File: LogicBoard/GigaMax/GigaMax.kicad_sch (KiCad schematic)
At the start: 40 parts, among them SW1 BOOT, SW3 RST, U12 STM32F407VGT6, U14 LM4128AMF-3.3, Y1 X50328MSB2GI

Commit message: moved libs and gigamax version
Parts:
- R2: footprint Resistor_SMD:R_0805_2012Metric -> Resistor_SMD:R_0603_1608Metric; MPN C26010 -> C22978

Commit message: cleanup
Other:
- moved on the sheet: C14, C15, U14

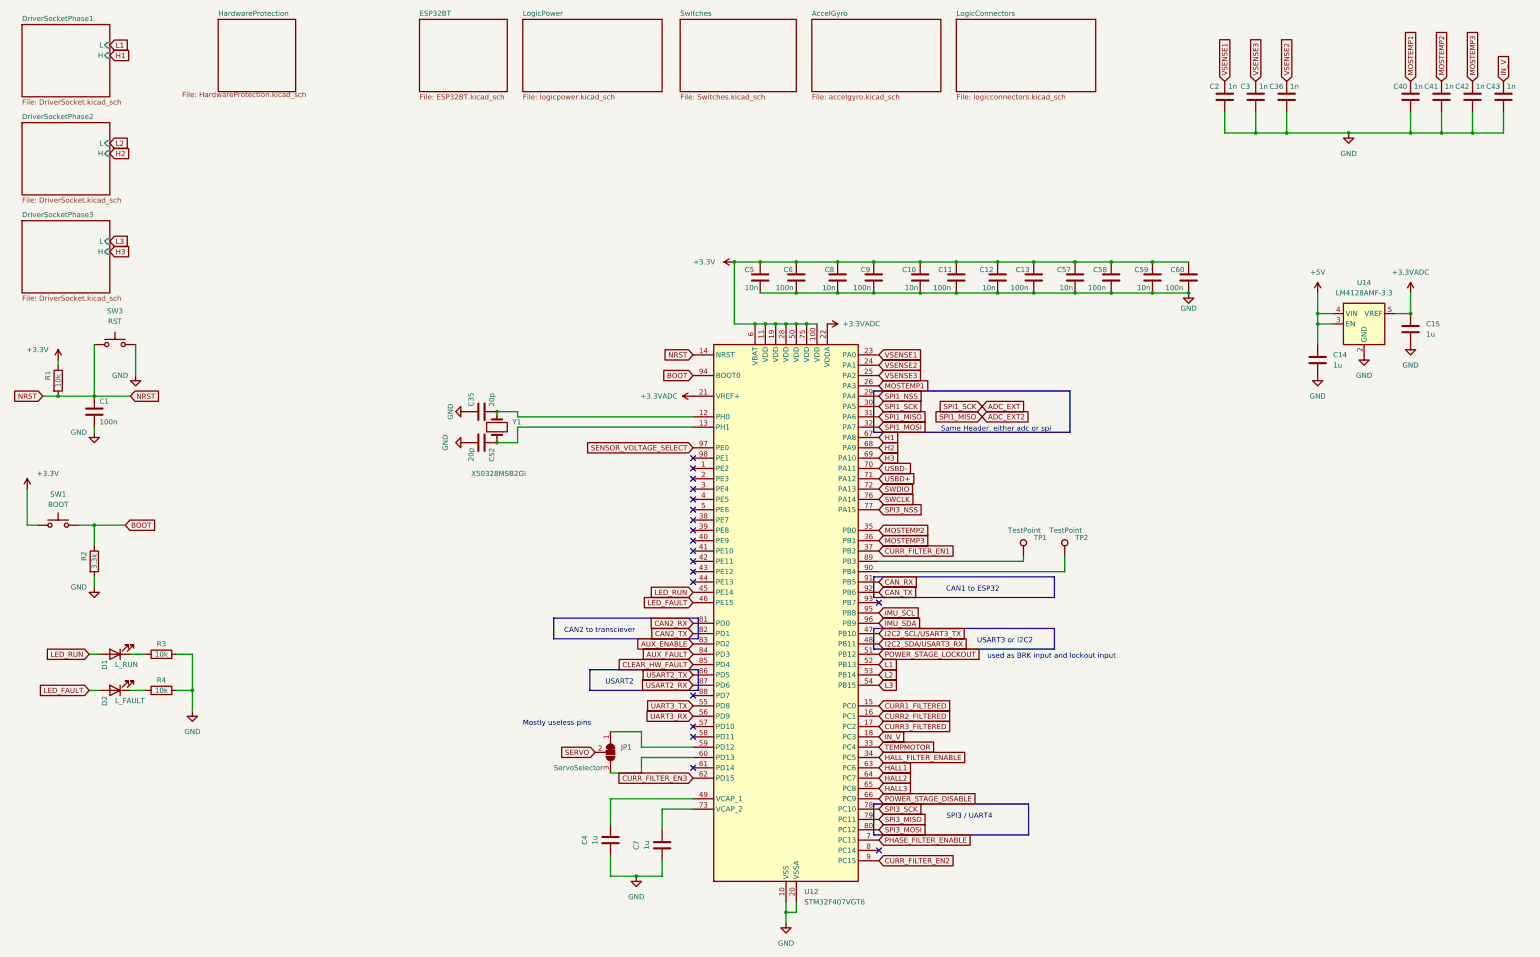
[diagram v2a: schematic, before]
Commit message: v2.8.0 - Small Hall sensors
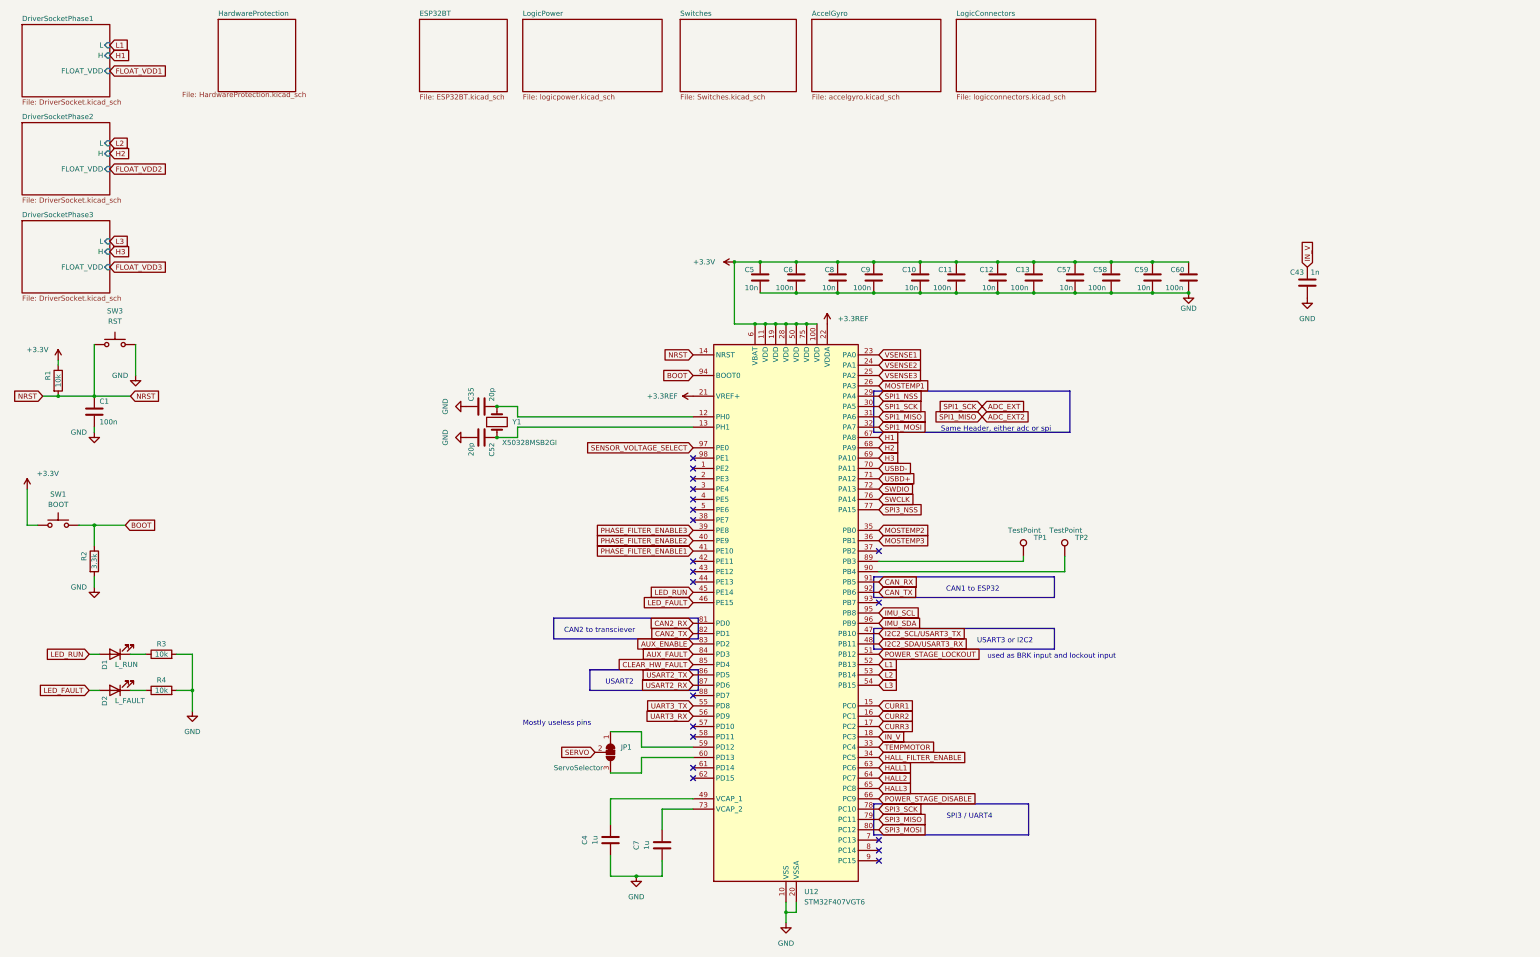
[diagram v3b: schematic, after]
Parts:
- removed C14, C15: 1u, GigaVescLibs:C_0603_1608Metric_L, symbol Device:C
- removed C2, C3, C36, C40, C41, C42: 1n, GigaVescLibs:C_0603_1608Metric_L, symbol Device:C
- removed U14: LM4128AMF-3.3, Package_TO_SOT_SMD:SOT-23-5, symbol Reference_Voltage:LM4128
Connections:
- net PHASE_FILTER_ENABLE3: now reaches U12.39 (PE8)
- net PHASE_FILTER_ENABLE2: now reaches U12.40 (PE9)
- net PHASE_FILTER_ENABLE1: now reaches U12.41 (PE10)
- net +3.3VADC renamed +3.3REF
- net CURR1_FILTERED renamed CURR1
- net CURR2_FILTERED renamed CURR2
- net CURR3_FILTERED renamed CURR3
- net CURR_FILTER_EN1: no longer names the net of U12.37 (PB2)
- net CURR_FILTER_EN2: no longer names the net of U12.9 (PC15)
- net CURR_FILTER_EN3: no longer names the net of U12.62 (PD15)
- net PHASE_FILTER_ENABLE: no longer names the net of U12.7 (PC13)
- no-connect marks 19 -> 20
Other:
- sheet DriverSocketPhase1 ports: added FLOAT_VDD; removed none
- sheet DriverSocketPhase2 ports: added FLOAT_VDD; removed none
- sheet DriverSocketPhase3 ports: added FLOAT_VDD; removed none
- moved on the sheet: C35, C43, C52, Y1
